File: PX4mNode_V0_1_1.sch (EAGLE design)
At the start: 128 parts, among them J2 DF13-4P-1.25V, J201 DF13C-6P-1.25V, J202 DF13C-6P-1.25V, J203 DF13C-6P-1.25V, J3 DF13C-4P-1.25V, J302 DF13C-4P-1.25V, J401 DF13C-4P-1.25V, J403 DF13C-7P-1.25V, J405 DF13C-4P-1.25V, J802 DF13C-3P-1.25V, M3_MOUNT1101 MOUNT-HOLE3.1MM, M3_MOUNT1102 MOUNT-HOLE3.1MM, M3_MOUNT1103 MOUNT-HOLE3.1MM, M3_MOUNT1104 MOUNT-HOLE3.1MM, U101 STM32F4X7VX, U2 MAX3051, U401 MAX3051, X101 3.2x2.5 mm / 24 MHz / 15 ppm

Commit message: Parts renumber
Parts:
- removed C1, C10, C8, C9: 22uF, SparkFun-Capacitors:22UF-16V-20%-(1210)
- removed C103: 8p, pixhawk2:CAP0402
- removed C12, C6, C7: 0u1, pixhawk2:CAP0402
- removed FMU-BOOT0: PAD.04, pixhawk2:PAD.04
- removed JP1, JP2: FIDUCIAL1.5X3, pixhawk2:FIDUCIAL1.5X3
- removed L2, L3, L6: NUF8402MN, PX4lite:NUF8402MN
- removed L5: KNH16C104DA5TS, PX4lite:KNH16C104DA5TS
- removed R1: 1K5, pixhawk2:RESISTOR0402-RES
- removed R4, R409: 120R, pixhawk2:RESISTOR0402-RES
- removed R609: 10K/0.1%, pixhawk2:RESISTOR0402-RES
- removed U$14: HEADER-3X1RA, PX4lite:HEADER-3X1RA
- removed U$4: PESD0402-140, pixhawk2:DIODE-TVS
- removed U$605: MIC5332, pixhawk2:MIC5332
- removed U2: MAX3051, pixhawk2:MAX3051MAX3051EKA
- added C101: 8p, pixhawk2:CAP0402
- added C701: 2u2, pixhawk2:CAP0603
- added C703: 10n, pixhawk2:CAP0402
- added C705, C708: 1u0, pixhawk2:CAP0603
- added C706: 10u/10V, pixhawk2:CAP0805
- added C711, C712: 0u1, pixhawk2:CAP0402
- added FMU-BOOT1101: PAD.04, pixhawk2:PAD.04
- added JP1101, JP1102: FIDUCIAL1.5X3, pixhawk2:FIDUCIAL1.5X3
- added L204, L205, L401, L406: KNH16C104DA5TS, PX4lite:KNH16C104DA5TS
- added R404: 1K5, pixhawk2:RESISTOR0402-RES
- added R405, R406: 10K/0.1%, pixhawk2:RESISTOR0402-RES
- added R804: 220R, pixhawk2:RESISTOR0402-RES
- added U$204, U$402, U$801: PESD0402-140, pixhawk2:DIODE-TVS
- added U402: MAX3051, pixhawk2:MAX3051MAX3051EKA
- C601: value 2u2 -> 22uF; device pixhawk2:CAP0603 -> SparkFun-Capacitors:22UF-16V-20%-(1210); PARTNO C1608Y5V1C225Z -> (none)
- C602: value 10n -> 0u1; PARTNO CC0402KRX7R7BB103 -> CC0402ZRY5V7BB104
- C603: value 1u0 -> 0u1; device pixhawk2:CAP0603 -> pixhawk2:CAP0402; PARTNO CC0603ZRY5V7BB105 -> CC0402ZRY5V7BB104
- C604: value 10u/10V -> 0u1; device pixhawk2:CAP0805 -> pixhawk2:CAP0402; PARTNO CC0805ZKY5V6BB106 -> CC0402ZRY5V7BB104
- C605: value 1u0 -> 22uF; device pixhawk2:CAP0603 -> SparkFun-Capacitors:22UF-16V-20%-(1210); PARTNO CC0603ZRY5V7BB105 -> (none)
- C606, C607: value 0u1 -> 22uF; device pixhawk2:CAP0402 -> SparkFun-Capacitors:22UF-16V-20%-(1210); PARTNO CC0402ZRY5V7BB104 -> (none)
- J401: value DF13C-4P-1.25V -> DF13C-7P-1.25V; device con-hirose-df13:DF13-4P-1.25V -> con-hirose-df13:DF13-7P-1.25V; PARTNO DF13C-4P-1.25V(20) -> DF13C-7P-1.25V(20)
- J403: value DF13C-7P-1.25V -> DF13C-4P-1.25V; device con-hirose-df13:DF13-7P-1.25V -> con-hirose-df13:DF13-4P-1.25V; PARTNO DF13C-7P-1.25V(20) -> DF13C-4P-1.25V(20)
- L201, L202, L402: value KNH16C104DA5TS -> NUF8402MN; device PX4lite:KNH16C104DA5TS -> PX4lite:NUF8402MN; PARTNO KNH16C104DA5TS -> (none)
- R407, R408: value 10K/0.1% -> 120R; PARTNO ERA-2AEB103X -> RC0402FR-07120RL
- R707: value 220R -> 10K/0.1%; PARTNO RC0402FR-07220RL -> ERA-2AEB103X
- U$201: value PESD0402-140 -> HEADER-3X1RA; device pixhawk2:DIODE-TVS -> PX4lite:HEADER-3X1RA; PARTNO PESD0402-140 -> (none)
- U$701: value PESD0402-140 -> MIC5332; device pixhawk2:DIODE-TVS -> pixhawk2:MIC5332; PARTNO PESD0402-140 -> MIC5332-SSYMT
- renumbered C1001 to C702, C1002 to C704, C1003 to C707, C1004 to C709, C13 to C301, C14 to C302, C15 to C710, C2 to C403, C3 to C404, C4 to C401, C5 to C503, C505 to C502, C506 to C501, C608 to C713, C609 to C714, C610 to C715, C611 to C716, C612 to C717, C613 to C718, D1 to D904, D2 to D902, D3 to D901, D5 to D903, J1 to J1001, J2 to J402, J3 to J404, J302 to J301, J802 to J801, JP3 to JP701, JP5 to JP901, L1 to L1001, L4 to L404, L7 to L405, LED701 to LED801, LED704 to LED802, R1002 to R703, R102 to R101, R2 to R403, R3 to R803, R5 to R702, R603 to R701, R606 to R704, R607 to R705, R608 to R706, R610 to R708, R611 to R709, R710 to R801, R711 to R805, R713 to R802, R918 to R902, R919 to R903, R922 to R901, S601 to S701, SJ1 to SJ403, SJ2 to SJ402, SJ3 to SJ401, U$1 to U$405, U$1002 to U$702, U$15 to U$602, U$16 to U$601, U$2 to U$501, U$3 to U$302, U$5 to U$301, U$604 to U$703, U$7 to U$403
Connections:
- net !FMU-LED_AMBER: now also R804.1; no longer R707.1
- net !SPI_EXT_NSS: now also J401.5; no longer J403.5
- net 5V_CAN_CONN: now also L406.P$1; no longer L403.P$1
- net 5V_S1_FILTERED: now also L203.P$2, U$202.C; no longer L201.P$2, U$201.C
- net 5V_S2_FILTERED: now also L204.P$2, U$203.C; no longer L202.P$2, U$202.C
- net 5V_S3_FILTERED: now also L205.P$2, U$204.C; no longer L203.P$2, U$203.C
- net CAN1_H: now also R408.1, U402.CANH; no longer R409.1, U401.CANH
- net CAN1_L: now also U402.CANL; no longer U401.CANL
- net CAN1_RX: now also U402.DOUT; no longer U401.DOUT
- net CAN1_TX: now also U402.DIN; no longer U401.DIN
- net CAN2_H: now also R407.1, U401.CANH; no longer R4.1, U2.CANH
- net CAN2_L: now also U401.CANL; no longer U2.CANL
- net CAN2_RX: now also U401.DOUT; no longer U2.DOUT
- net CAN2_TX: now also U401.DIN; no longer U2.DIN
- net FMU-!RESET: now also U$701.POR2; no longer U$605.POR2
- net FMU-BOOT0: now also FMU-BOOT1101.P$1; no longer FMU-BOOT0.P$1
- net FMU-I2C1_SCL: now also L402G$8.P$1, R402.1; no longer L6G$8.P$1, R401.1
- net FMU-I2C1_SDA: now also L402G$7.P$1, R404.1; no longer L6G$7.P$1, R402.1
- net FMU-I2C2_SCL: now also L402G$2.P$1, R401.1; no longer L6G$2.P$1, R1.1
- net FMU-I2C2_SDA: now also L402G$1.P$1; no longer L6G$1.P$1
- net FMU-UART7_RX: now also L201G$5.P$1; no longer L3G$5.P$1
- net FMU-UART7_TX: now also L201G$6.P$1; no longer L3G$6.P$1
- net FMU-USART2_CTS: now also L202G$8.P$1; no longer L2G$8.P$1
- net FMU-USART2_RTS: now also L202G$7.P$1; no longer L2G$7.P$1
- net FMU-USART2_RX: now also L202G$5.P$1; no longer L2G$5.P$1
- net FMU-USART2_TX: now also L202G$6.P$1; no longer L2G$6.P$1
- net FMU-USART3_CTS: now also L202G$2.P$1; no longer L2G$2.P$1
- net FMU-USART3_RTS: now also L202G$1.P$1; no longer L2G$1.P$1
- net FMU-USART3_RX: now also L202G$3.P$1; no longer L2G$3.P$1
- net FMU-USART3_TX: now also L202G$4.P$1; no longer L2G$4.P$1
- net FMU-VDD_3V3: now also C705.1, C706.1, C711.1, C712.1, R404.2, U$701.VOUT2, U$801.C, U402.VCC; no longer C603.1, C604.1, C606.1, C607.1, R1.2, U$605.VOUT2, U$701.C, U2.VCC
- net FMU_AUX_ADC1: now also R405.1; no longer R408.1
- net FMU_AUX_ADC1_PROT: now also R405.2; no longer R408.2
- net FMU_AUX_ADC2: now also R406.1; no longer R407.1
- net FMU_AUX_ADC2_PROT: now also R406.2; no longer R407.2
- net GND: now also C101.2, C102.1, C602.2, C701.2, C703.1, C705.2, C706.2, C708.2, C711.2, C712.2, J401.7, J403.4, L201G$9.GND, L202G$9.GND, L204.P$3, L205.P$3, L401.P$3, L402G$9.GND, L406.P$3, U$201.3, U$204.A, U$402.A, U$701.GND, U$801.A, U402.GND, U402.RS, U402.SHDN; no longer C1.2, C10.2, C102.2, C103.1, C12.2, C6.2, C602.1, C7.2, C8.2, C9.2, J401.4, J403.7, L201.P$3, L202.P$3, L2G$9.GND, L3G$9.GND, L402.P$3, L5.P$3, L6G$9.GND, U$14.3, U$201.A, U$4.A, U$605.GND, U$701.A, U2.GND, U2.RS, U2.SHDN
- net GPIO_EXT_1: now also J401.6; no longer J403.6
- net N$1: now also C102.2; no longer C103.2
- net N$11: now also C703.2, U$701.CSET; no longer C602.2, U$605.CSET
- net N$13: now also R804.2; no longer R707.2
- net N$18: now also L201G$3.P$2, L201G$4.P$2, U$201.1; no longer L3G$3.P$2, L3G$4.P$2, U$14.1
- net N$2: now also C101.1; no longer C102.1
- net N$20: now also L402G$1.P$2; no longer L6G$1.P$2
- net N$21: now also L403.P$2, U$401.C; no longer L5.P$2, U$4.C
- net N$22: now also R408.2; no longer R409.2
- net N$27: now also C603.1; no longer C6.1
- net N$29: now also R407.2; no longer R4.2
- net N$33: now also J403.2, L402G$8.P$2; no longer J401.2, L6G$8.P$2
- net N$37: now also J403.3, L402G$7.P$2; no longer J401.3, L6G$7.P$2
- net N$4: now also L402G$2.P$2; no longer L6G$2.P$2
- net N$41: now also J401.1, L401.P$2; no longer J403.1, L402.P$2
- net N$42: now also J403.1, U$402.C; no longer J401.1, U$401.C
- net N$48: now also L406.P$2; no longer L403.P$2
- net PPM_INPUT: now also L201G$3.P$1; no longer L3G$3.P$1
- net SERIAL1_CTS: now also L202G$8.P$2; no longer L2G$8.P$2
- net SERIAL1_RTS: now also L202G$7.P$2; no longer L2G$7.P$2
- net SERIAL1_RX: now also L202G$5.P$2; no longer L2G$5.P$2
- net SERIAL1_TX: now also L202G$6.P$2; no longer L2G$6.P$2
- net SERIAL2_CTS: now also L202G$2.P$2; no longer L2G$2.P$2
- net SERIAL2_RTS: now also L202G$1.P$2; no longer L2G$1.P$2
- net SERIAL2_RX: now also L202G$3.P$2; no longer L2G$3.P$2
- net SERIAL2_TX: now also L202G$4.P$2; no longer L2G$4.P$2
- net SERIAL3_RX: now also L201G$5.P$2; no longer L3G$5.P$2
- net SERIAL3_TX: now also L201G$6.P$2; no longer L3G$6.P$2
- net SPEKTRUM_RX: now also L201G$4.P$1; no longer L3G$4.P$1
- net SPI_EXT_MISO: now also J401.3; no longer J403.3
- net SPI_EXT_MOSI: now also J401.4; no longer J403.4
- net SPI_EXT_SCK: now also J401.2; no longer J403.2
- net VDD_3V3_SPEKTRUM: now also C708.1, U$201.2, U$701.VOUT1; no longer C605.1, U$14.2, U$605.VOUT1
- net VDD_3V3_SPEKTRUM_EN: now also U$701.EN1; no longer U$605.EN1
- net VDD_5V: now also C604.1, C605.1, C606.1, C607.1, C701.1, R707.2, U$701.EN2, U$701.VIN; no longer C10.1, C601.1, C7.1, C8.1, C9.1, R609.2, U$605.EN2, U$605.VIN
- net VDD_5V_PERIPH: now also L204.P$1, L205.P$1, L401.P$1, L403.P$1; no longer L201.P$1, L202.P$1, L402.P$1, L5.P$1
- net VDD_5V_SENS: now also R707.1; no longer R609.1
- net VDD_IN: now also C601.1, C602.1; no longer C1.1, C12.1
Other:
- note removed: "Peripherals Power Supply"

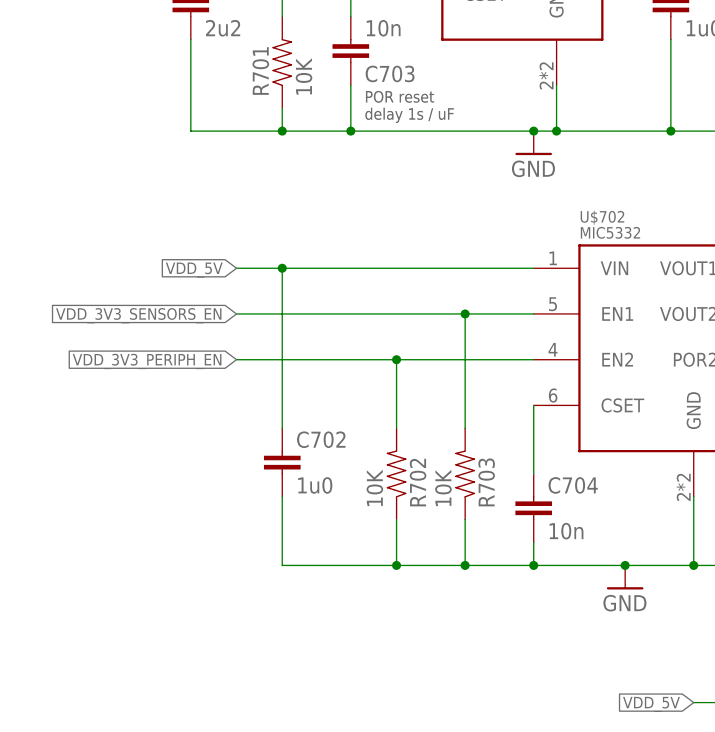
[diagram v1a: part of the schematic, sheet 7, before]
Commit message: Sensor 3V3 supply changed to default enabled
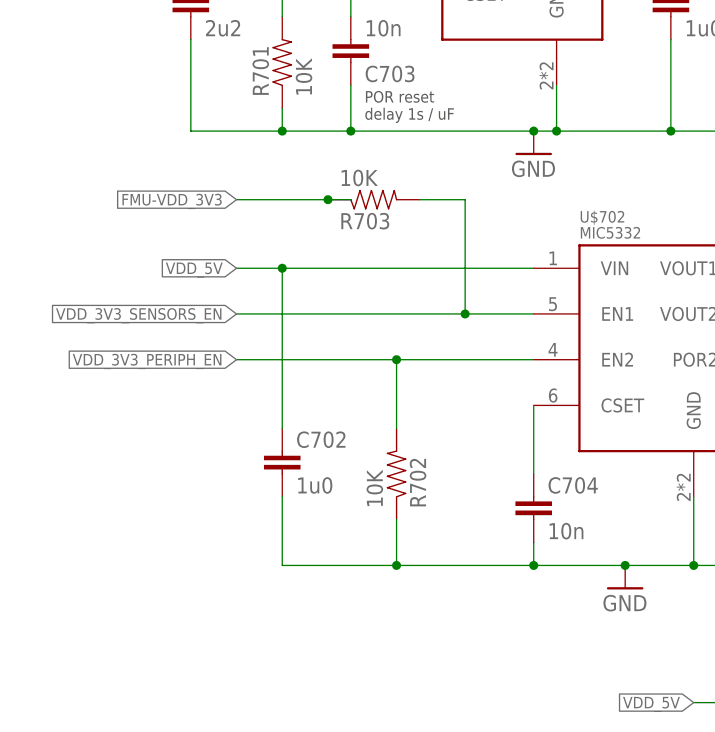
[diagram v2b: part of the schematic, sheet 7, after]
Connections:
- net FMU-VDD_3V3: now also R703.1
- net GND: no longer R703.1
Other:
- moved on the sheet: R703
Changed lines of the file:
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@@
 <attribute name="PARTNO" x="81.28" y="104.14" size="1.778" layer="96" display="off"/>
 </instance>
-<instance part="R703" gate="G$1" x="60.96" y="86.36" smashed="yes" rot="MR90">
-<attribute name="PARTNO" x="60.96" y="86.36" size="1.778" layer="96" rot="MR90" display="off"/>
-<attribute name="NAME" x="62.4586" y="82.55" size="1.778" layer="95" rot="MR90"/>
-<attribute name="VALUE" x="57.658" y="82.55" size="1.778" layer="96" rot="MR90"/>
+<instance part="R703" gate="G$1" x="50.8" y="116.84" smashed="yes" rot="MR180">
+<attribute name="PARTNO" x="50.8" y="116.84" size="1.778" layer="96" rot="MR180" display="off"/>
+<attribute name="NAME" x="46.99" y="115.3414" size="1.778" layer="95" rot="MR180"/>
+<attribute name="VALUE" x="46.99" y="120.142" size="1.778" layer="96" rot="MR180"/>
 </instance>
 <instance part="R702" gate="G$1" x="53.34" y="86.36" smashed="yes" rot="MR90">
@@
 <junction x="68.58" y="76.2"/>
 <pinref part="U$702" gate="G$1" pin="GND"/>
-<pinref part="R703" gate="G$1" pin="1"/>
-<wire x1="53.34" y1="76.2" x2="60.96" y2="76.2" width="0.1524" layer="91"/>
-<wire x1="60.96" y1="76.2" x2="68.58" y2="76.2" width="0.1524" layer="91"/>
-<wire x1="60.96" y1="76.2" x2="60.96" y2="81.28" width="0.1524" layer="91"/>
-<junction x="60.96" y="76.2"/>
+<wire x1="53.34" y1="76.2" x2="68.58" y2="76.2" width="0.1524" layer="91"/>
 <pinref part="R702" gate="G$1" pin="1"/>
 <wire x1="53.34" y1="81.28" x2="53.34" y2="76.2" width="0.1524" layer="91"/>
@@
 <pinref part="C706" gate="G$1" pin="1"/>
 </segment>
+<segment>
+<label x="35.56" y="116.84" size="1.27" layer="95" rot="R180" xref="yes"/>
+<wire x1="48.26" y1="116.84" x2="45.72" y2="116.84" width="0.1524" layer="91"/>
+<pinref part="R703" gate="G$1" pin="1"/>
+<wire x1="45.72" y1="116.84" x2="35.56" y2="116.84" width="0.1524" layer="91"/>
+<junction x="45.72" y="116.84"/>
+</segment>
 </net>
 <net name="FMU-BOOT0" class="0">
@@
 <wire x1="68.58" y1="104.14" x2="60.96" y2="104.14" width="0.1524" layer="91"/>
 <pinref part="R703" gate="G$1" pin="2"/>
-<wire x1="60.96" y1="104.14" x2="60.96" y2="91.44" width="0.1524" layer="91"/>
+<wire x1="60.96" y1="104.14" x2="60.96" y2="116.84" width="0.1524" layer="91"/>
+<wire x1="60.96" y1="116.84" x2="55.88" y2="116.84" width="0.1524" layer="91"/>
 <label x="35.56" y="104.14" size="1.27" layer="95" rot="R180" xref="yes"/>
 <junction x="60.96" y="104.14"/>
